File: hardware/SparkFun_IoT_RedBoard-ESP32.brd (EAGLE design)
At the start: 68.6 x 58.4 mm, 229 parts, among them J1 5.5x2.1mm Barrel, J13 QWIIC_RIGHT_ANGLE, J15 MICRO-SD-PUSH-PUSH-EXT-PIN, J2 USB-C, J3 USB_SOLDER_PADS, J5 M10NO_SILK, Q1 MBT3904DW1T1, Q11 20V/4.2A/52mΩ/1.4W, Q13 20V/4.2A/52mΩ/1.4W, Q3 20V/4.2A/52mΩ/1.4W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

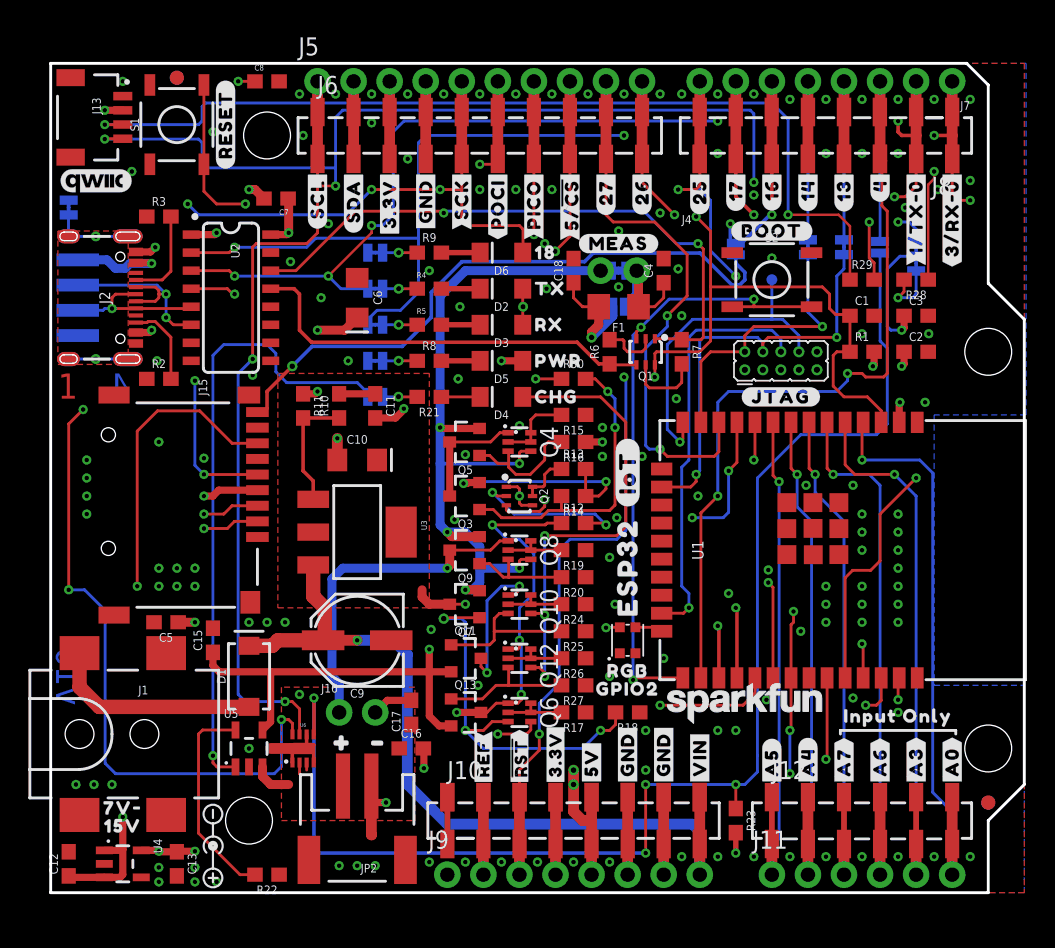
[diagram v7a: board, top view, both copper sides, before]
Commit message: Design review updates
Add decoupling cap for WS2812
Move SparkFun logo in top silk
Add GND via for 3V regulator
Change I2C label to use superscript 2
Remove extraneous lines in schematic
Add warnings about ESP32 boot pins and ADC2/WiFi to schematic
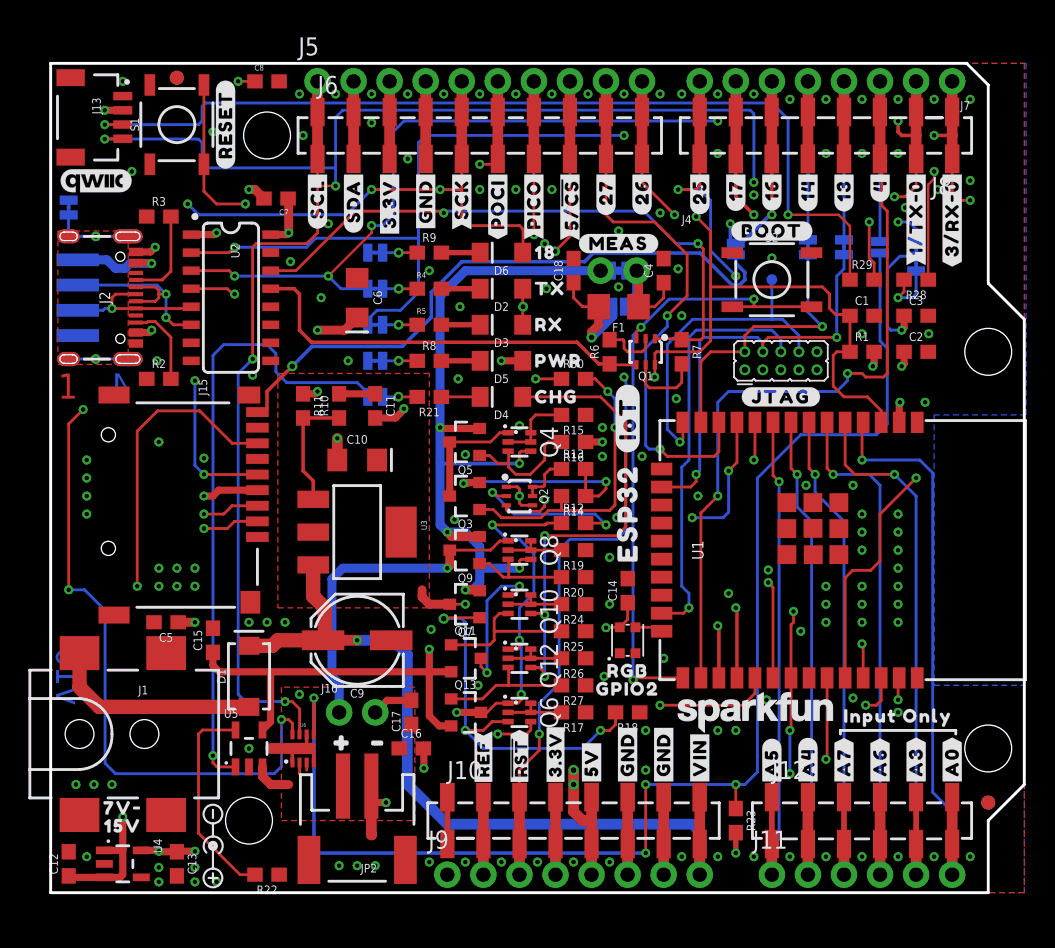
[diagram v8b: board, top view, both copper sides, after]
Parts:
- removed U$89: (no value), output-ESP32:#I2C#1855
- added C14: 0.1uF, SparkFun-Capacitors:0603
- added U$82: (no value), output:#I�C#0
- moved U$100 3.81 mm to (40.6, 33.4)
- moved U$48 3.81 mm to (40.6, 22.2)
- moved LOGO1 0.99 mm to (49.7, 12.7)
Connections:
- net 3.3V: now also C14.1
- net GND: now also C14.2
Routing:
- net 3.3V: track 47.9 -> 49.9 mm
- net GND: vias 152 -> 153
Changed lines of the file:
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@@
 <attribute name="PROD_ID" value="DIO-09912" x="31.75" y="41.275" size="1.778" layer="27" rot="R180" display="off"/>
 </element>
-<element name="LOGO1" library="SparkFun-Aesthetics" package="SFE_LOGO_NAME_.1" value="SFE_LOGO_NAME.1_INCH" x="48.895" y="13.335" smashed="yes"/>
+<element name="LOGO1" library="SparkFun-Aesthetics" package="SFE_LOGO_NAME_.1" value="SFE_LOGO_NAME.1_INCH" x="49.657" y="12.7" smashed="yes"/>
 <element name="LOGO2" library="SparkFun-Aesthetics" package="QWIIC_5MM" value="QWIIC_LOGO_5MM" x="3.175" y="50.165" smashed="yes"/>
 <element name="LOGO3" library="SparkFun-Aesthetics" package="OSHW-LOGO-MINI" value="OSHW-LOGOMINI" x="2.286" y="5.08" smashed="yes" rot="MR0"/>
@@
 <element name="U$45" library="output-ESP32" package="#BATT#1848" value="" x="21.59" y="14.859" smashed="yes" rot="MR0"/>
 <element name="U$46" library="output-ESP32" package="#JTAG#1847" value="" x="51.435" y="34.925" smashed="yes" rot="MR0"/>
-<element name="U$48" library="output-ESP32" package="ESP321855" value="" x="40.64" y="18.415" smashed="yes" rot="R90"/>
+<element name="U$48" library="output-ESP32" package="ESP321855" value="" x="40.64" y="22.225" smashed="yes" rot="R90"/>
 <element name="U$50" library="output-ESP32" package="#39#A3#321862" value="" x="60.96" y="1.778" smashed="yes" rot="MR90"/>
 <element name="U$51" library="output-ESP32" package="#36#A0#321862" value="" x="63.5" y="1.778" smashed="yes" rot="MR90"/>
@@
 <element name="U$86" library="output-ESP32" package="#1849" value="" x="20.32" y="10.541" smashed="yes" rot="MR0"/>
 <element name="U$88" library="output-ESP32" package="#1850" value="" x="22.86" y="10.541" smashed="yes" rot="MR0"/>
-<element name="U$89" library="output-ESP32" package="#I2C#1855" value="" x="60.96" y="43.434" smashed="yes" rot="MR90"/>
 <element name="U$90" library="output-ESP32" package="##ALERT##1852" value="" x="58.42" y="44.704" smashed="yes" rot="MR90"/>
 <element name="U$91" library="output-ESP32" package="#TMS#1854" value="" x="53.34" y="44.577" smashed="yes" rot="MR90"/>
@@
 <element name="TP1" library="SparkFun-Connectors" package="PAD.03X.03" value="TEST-POINT3" x="50.8" y="43.18" smashed="yes" rot="MR0"/>
 <element name="U$98" library="SparkFun-Aesthetics" package="REDBOARD_LOGO" value="" x="46.99" y="21.59" smashed="yes" rot="MR0"/>
-<element name="U$100" library="output-ESP32" package="#IOT#132321869" value="" x="40.64" y="29.591" smashed="yes" rot="R90"/>
+<element name="U$100" library="output-ESP32" package="#IOT#132321869" value="" x="40.64" y="33.401" smashed="yes" rot="R90"/>
 <element name="U$93" library="output-ESP32" package="ESP32321856" value="" x="41.275" y="20.193" smashed="yes" rot="MR0"/>
 <element name="U$47" library="output-ESP32" package="#IOT#132321874" value="" x="27.432" y="31.369" smashed="yes" rot="MR0"/>
@@
 <element name="U$113" library="output" package="GPIO20" value="" x="40.64" y="14.351" smashed="yes"/>
 <element name="U$52" library="output" package="#33#A5#0" value="" x="50.8" y="1.778" smashed="yes" rot="MR90"/>
+<element name="C14" library="SparkFun-Capacitors" package="0603" value="0.1uF" x="40.64" y="21.2725" smashed="yes" rot="R90">
+<attribute name="NAME" x="39.878" y="21.2725" size="0.6096" layer="25" font="vector" ratio="20" rot="R90" align="bottom-center"/>
+<attribute name="PROD_ID" value="CAP-00810" x="40.64" y="22.5425" size="1.778" layer="27" rot="R90" display="off"/>
+<attribute name="VALUE" x="41.402" y="21.2725" size="0.6096" layer="27" font="vector" ratio="20" rot="R90" align="top-center"/>
+</element>
+<element name="U$82" library="output" package="#I�C#0" value="" x="60.96" y="43.434" smashed="yes" rot="MR90"/>
 </elements>
 <signals>
@@
 <via x="48.26" y="11.43" extent="1-16" drill="0.3048"/>
 <via x="46.99" y="11.43" extent="1-16" drill="0.3048"/>
-<via x="39.37" y="15.24" extent="1-16" drill="0.3048"/>
+<via x="38.989" y="15.24" extent="1-16" drill="0.3048"/>
 <via x="43.18" y="16.51" extent="1-16" drill="0.3048"/>
-<via x="39.751" y="20.32" extent="1-16" drill="0.3048"/>
+<via x="39.37" y="20.32" extent="1-16" drill="0.3048"/>
 <via x="16.51" y="19.05" extent="1-16" drill="0.3048"/>
 <via x="15.24" y="19.05" extent="1-16" drill="0.3048"/>
@@
 <via x="19.05" y="41.91" extent="1-16" drill="0.3048"/>
 <via x="34.798" y="45.72" extent="1-16" drill="0.3048"/>
+<contactref element="C14" pad="2"/>
+<via x="2.54" y="2.54" extent="1-16" drill="0.3048"/>
 </signal>
 <signal name="VIN" class="1">
@@
 <wire x1="33.25" y1="42.545" x2="33.25" y2="41.299" width="0.2032" layer="1"/>
 <wire x1="33.25" y1="41.299" x2="33.274" y2="41.275" width="0.2032" layer="1"/>
+<contactref element="C14" pad="1"/>
+<wire x1="40.09" y1="18.695" x2="40.64" y2="19.245" width="0.2032" layer="1"/>
+<wire x1="40.64" y1="19.245" x2="40.64" y2="20.4225" width="0.2032" layer="1"/>
 </signal>
 <signal name="ESP32_SCL">
